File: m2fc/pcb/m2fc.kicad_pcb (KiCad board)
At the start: 4 copper layers, 100 x 70 mm, 342 parts, among them IC101 ADP3335, IC102 STM32F405VGT, IC201 AD8226, IC202 AD8656, IC203 AD8541, IC204 AD8226, IC205 AD8656, IC206 AD8541, IC207 AD8226, IC208 AD8656, IC209 AD8541, IC301 ADXL375, IC302 ADXL345, IC303 MS5611-01BA03, IC304 HMC5883L, IC305 L3G4200D, IC401 ADuM5201, IC402 ADuM1201, IC601 AD8495, IC602 AD8656, IC603 AD8495, IC604 AD8656, IC605 AD8495, IC606 AD8656, P101 CONN_2, P102 CONN_2, P103 CONN_2, P104 SWD, P201 CONN_4, P202 CONN_4, P203 CONN_4, P401 CONN_4, P402 CONN_2, P403 CONN_4, P501 CONN_2, P502 CONN_2, P503 CONN_2, P601 CONN_2, P602 CONN_2, P603 CONN_2, Q501 MOSFET_P, Q502 MOSFET_N, Q503 MOSFET_P, Q504 MOSFET_N, Q505 MOSFET_P, Q506 MOSFET_N, U106 MICROSD, X101 8M

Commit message: layout going ok so far...
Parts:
- added M3_MOUNT: VAL**, m2fc:M3_MOUNT, F.Cu at (57.8, 42.8)
- added M3_MOUNT: VAL**, m2fc:M3_MOUNT, F.Cu at (76.6, 34.4)
- added M3_MOUNT: VAL**, m2fc:M3_MOUNT, F.Cu at (126.2, 34.2)
- added M3_MOUNT: VAL**, m2fc:M3_MOUNT, F.Cu at (144.4, 45.2)
- added M3_MOUNT: VAL**, m2fc:M3_MOUNT, F.Cu at (145.4, 95.4)
- added M3_MOUNT: VAL**, m2fc:M3_MOUNT, F.Cu at (45.6, 79.2)
- moved C630 220.9 mm to (64.8, 65.4), turned to 270 degrees
- moved R607 211.6 mm to (66.2, 45.2), turned to 90 degrees
- moved C619 210.3 mm to (64.8, 54.6), turned to 270 degrees
- moved C620 206.0 mm to (74.0, 53.0), turned to 90 degrees
- moved R613 205.7 mm to (64.2, 57.2), turned to 180 degrees
- moved R618 201.6 mm to (75.6, 65.2), turned to 180 degrees
- moved C616 198.9 mm to (76.8, 53.0), turned to 90 degrees
- moved C623 197.7 mm to (68.4, 61.0), turned to 90 degrees
- moved R612 197.6 mm to (74.0, 55.8)
- moved R601 196.1 mm to (64.2, 42.6), turned to 180 degrees
- moved R603 195.4 mm to (72.6, 40.4), turned to 180 degrees
- moved C615 195.2 mm to (75.4, 53.0), turned to 90 degrees
- moved R614 194.9 mm to (66.2, 56.2), turned to 90 degrees
- moved C611 193.2 mm to (62.6, 48.0)
- moved C626 193.1 mm to (75.4, 63.8), turned to 90 degrees
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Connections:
- C611 pad 1: Net-(C608-Pad2) -> GND
- C611 pad 2: GND -> Net-(C608-Pad2)
- C622 pad 1: Net-(C619-Pad2) -> GND
- C622 pad 2: GND -> Net-(C619-Pad2)
- C633 pad 1: Net-(C630-Pad2) -> GND
- C633 pad 2: GND -> Net-(C630-Pad2)
- D407 pad 1: /IO/LED_C -> GND
- D407 pad 2: GND -> /IO/LED_C
- IC102 pad 45: Net-(IC102-Pad45) -> /IMU/GYRO_DRDY
- IC102 pad 46: /IMU/MAGNO_DRDY -> /IMU/GYRO_INT1
- IC102 pad 47: /IMU/MAGNO_SCL -> /IMU/GYRO_SCL
- IC102 pad 48: /IMU/MAGNO_SDA -> /IMU/GYRO_SDA
- IC102 pad 95: /IMU/GYRO_SCL -> /IMU/MAGNO_SCL
- IC102 pad 96: /IMU/GYRO_SDA -> /IMU/MAGNO_SDA
- IC102 pad 97: /IMU/GYRO_DRDY -> /IMU/MAGNO_DRDY
- IC102 pad 98: /IMU/GYRO_INT1 -> Net-(IC102-Pad98)
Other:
- board size 100 x 70 mm -> 108.8 x 70 mm

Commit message: about to do something dangerous to pcb
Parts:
- removed M3_MOUNT (x6): VAL**, m2fc:M3_MOUNT
- added U107: MOUNT, m2fc:M3_MOUNT, F.Cu at (45.6, 79.2)
- added U108: MOUNT, m2fc:M3_MOUNT, F.Cu at (76.6, 34.4)
- added U109: MOUNT, m2fc:M3_MOUNT, F.Cu at (126.2, 34.2)
- added U110: MOUNT, m2fc:M3_MOUNT, F.Cu at (145.4, 95.4)
- added U111: MOUNT, m2fc:M3_MOUNT, F.Cu at (144.4, 45.2)
- added U112: MOUNT, m2fc:M3_MOUNT, F.Cu at (57.8, 42.8)
- Q501, Q502, Q503, Q504, Q505, Q506: footprint m2fc:SOT-23 -> m2fc:SOT-23-MOSFET
- R505, R512, R519: moved to F.Cu
- moved R511 81.7 mm to (124.2, 70.4), turned to 270 degrees
- moved R516 81.2 mm to (131.0, 70.4), turned to 270 degrees
- moved R509 76.5 mm to (122.8, 70.4), turned to 270 degrees
- moved TP501 76.1 mm to (120.8, 81.0)
- moved TP508 73.1 mm to (132.4, 69.6)
- moved R518 71.2 mm to (132.4, 70.4), turned to 270 degrees
- moved R501 66.3 mm to (118.6, 81.0), turned to 90 degrees
- moved R510 63.9 mm to (127.4, 75.4), turned to 90 degrees
- moved R517 63.9 mm to (135.6, 75.4), turned to 90 degrees
- moved R515 63.6 mm to (134.2, 75.4), turned to 90 degrees
- moved TP505 62.5 mm to (124.2, 69.6)
- moved TP509 62.4 mm to (148.0, 102.0)
- moved TP504 61.4 mm to (128.2, 75.4)
- moved R508 60.3 mm to (126.0, 75.4), turned to 90 degrees
- moved R502 59.4 mm to (115.2, 76.0), turned to 270 degrees
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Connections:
- P102 pad 1: GND -> Net-(P102-Pad1)
- P102 pad 2: Net-(P102-Pad2) -> GND
- P103 pad 1: Net-(P102-Pad2) -> +BATT
- P103 pad 2: +BATT -> Net-(P102-Pad1)

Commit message: paid off woo
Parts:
- added C124: 2µ2, m2fc:C0603, F.Cu at (93.6, 76.8)
- added C125: 1n, m2fc:C0603, F.Cu at (88.8, 79.2)
- added C126: 2µ2, m2fc:C0603, F.Cu at (85.6, 76.8)
- added IC103: ADP3335, m2fc:MSOP8, F.Cu at (87.4, 75.8)
- added TP111: TESTPAD, m2fc:TESTPAD, F.Cu at (87.4, 75.0)
- moved R102 141.8 mm to (96.4, 75.6), turned to 270 degrees
- moved R108 137.5 mm to (90.6, 67.4), turned to 90 degrees
- moved R101 135.4 mm to (95.0, 77.2), turned to 90 degrees
- moved C116 134.8 mm to (98.4, 57.2), turned to 90 degrees
- moved C117 133.7 mm to (93.8, 70.6), turned to 180 degrees
- moved C101 130.2 mm to (93.4, 74.2)
- moved C118 126.1 mm to (93.8, 72.0), turned to 180 degrees
- moved C121 124.2 mm to (89.2, 62.8), turned to 270 degrees
- moved C115 124.0 mm to (99.0, 76.4)
- moved C110 123.0 mm to (113.2, 60.4)
- moved C123 121.8 mm to (89.2, 67.4), turned to 90 degrees
- moved C114 121.1 mm to (111.0, 77.0)
- moved C113 116.0 mm to (93.8, 69.2), turned to 180 degrees
- moved GS102 113.5 mm to (118.0, 59.0), turned to 90 degrees
- moved C122 112.4 mm to (92.2, 67.8)
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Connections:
- C117 pad 1: +3.3V -> VAA
- C118 pad 1: +3.3V -> VAA
- C204 pad 1: +3.3V -> VAA
- C205 pad 1: +3.3V -> VAA
- C206 pad 1: +3.3V -> VAA
- C209 pad 2: +3.3V -> VAA
- C210 pad 2: +3.3V -> VAA
- C211 pad 2: +3.3V -> VAA
- C212 pad 1: +3.3V -> VAA
- C213 pad 1: +3.3V -> VAA
- C217 pad 1: +3.3V -> VAA
- C218 pad 1: +3.3V -> VAA
- C219 pad 1: +3.3V -> VAA
- C222 pad 2: +3.3V -> VAA
- C223 pad 2: +3.3V -> VAA
- C224 pad 2: +3.3V -> VAA
- C225 pad 1: +3.3V -> VAA
- C226 pad 1: +3.3V -> VAA
- C230 pad 1: +3.3V -> VAA
- C231 pad 1: +3.3V -> VAA
- C232 pad 1: +3.3V -> VAA
- C235 pad 2: +3.3V -> VAA
- C236 pad 2: +3.3V -> VAA
- C237 pad 2: +3.3V -> VAA
- C238 pad 1: +3.3V -> VAA
- C239 pad 1: +3.3V -> VAA
- C601 pad 1: +3.3V -> VAA
- C602 pad 1: +3.3V -> VAA
- C604 pad 1: +3.3V -> VAA
- C605 pad 1: +3.3V -> VAA
- C612 pad 1: +3.3V -> VAA
- C613 pad 1: +3.3V -> VAA
- C615 pad 1: +3.3V -> VAA
- C616 pad 1: +3.3V -> VAA
- C623 pad 1: +3.3V -> VAA
- C624 pad 1: +3.3V -> VAA
- C626 pad 1: +3.3V -> VAA
- C627 pad 1: +3.3V -> VAA
- D201 pad 2: +3.3V -> VAA
- D203 pad 2: +3.3V -> VAA
- D205 pad 2: +3.3V -> VAA
- IC102 pad 21: +3.3V -> VAA
- IC102 pad 22: +3.3V -> VAA
- IC102 pad 69: Net-(IC102-Pad69) -> /SJ1
- IC102 pad 7: /SJ1 -> Net-(IC102-Pad7)
- IC102 pad 70: Net-(IC102-Pad70) -> /SJ2
- IC102 pad 71: Net-(IC102-Pad71) -> /SJ3
- IC102 pad 8: /SJ2 -> Net-(IC102-Pad8)
- IC102 pad 9: /SJ3 -> Net-(IC102-Pad9)
- IC201 pad 8: +3.3V -> VAA
- IC202 pad 4: +3.3V -> VAA
- IC203 pad 5: +3.3V -> VAA
- IC204 pad 8: +3.3V -> VAA
- IC205 pad 4: +3.3V -> VAA
- IC206 pad 5: +3.3V -> VAA
- IC207 pad 8: +3.3V -> VAA
- IC208 pad 4: +3.3V -> VAA
- IC209 pad 5: +3.3V -> VAA
- IC601 pad 7: +3.3V -> VAA
- IC602 pad 4: +3.3V -> VAA
- IC603 pad 7: +3.3V -> VAA
- IC604 pad 4: +3.3V -> VAA
- IC605 pad 7: +3.3V -> VAA
- IC606 pad 4: +3.3V -> VAA
- P201 pad 4: +3.3V -> VAA
- P202 pad 4: +3.3V -> VAA
- P203 pad 4: +3.3V -> VAA
- R202 pad 1: +3.3V -> VAA
- R210 pad 1: +3.3V -> VAA
- R218 pad 1: +3.3V -> VAA

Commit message: omg layout done
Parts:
- moved C301 131.3 mm to (95.6, 83.2)
- moved R304 129.4 mm to (93.4, 59.8), turned to 90 degrees
- moved R301 129.1 mm to (102.2, 83.2), turned to 90 degrees
- moved C310 126.0 mm to (105.2, 80.2), turned to 180 degrees
- moved C314 122.6 mm to (89.2, 55.8), turned to 90 degrees
- moved C302 121.6 mm to (100.2, 83.2), turned to 180 degrees
- moved R306 119.3 mm to (94.8, 59.8), turned to 90 degrees
- moved C307 119.1 mm to (101.4, 55.8), turned to 90 degrees
- moved R307 117.1 mm to (108.0, 56.0), turned to 90 degrees
- moved R305 115.7 mm to (103.6, 81.6)
- moved C312 114.6 mm to (90.6, 54.2), turned to 270 degrees
- moved TP303 113.5 mm to (99.0, 77.6)
- moved C313 109.3 mm to (108.0, 76.8), turned to 270 degrees
- moved C311 108.8 mm to (109.4, 76.8), turned to 270 degrees
- moved TP307 108.7 mm to (103.0, 76.8)
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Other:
- board size 108.8 x 70 mm -> 100 x 70 mm

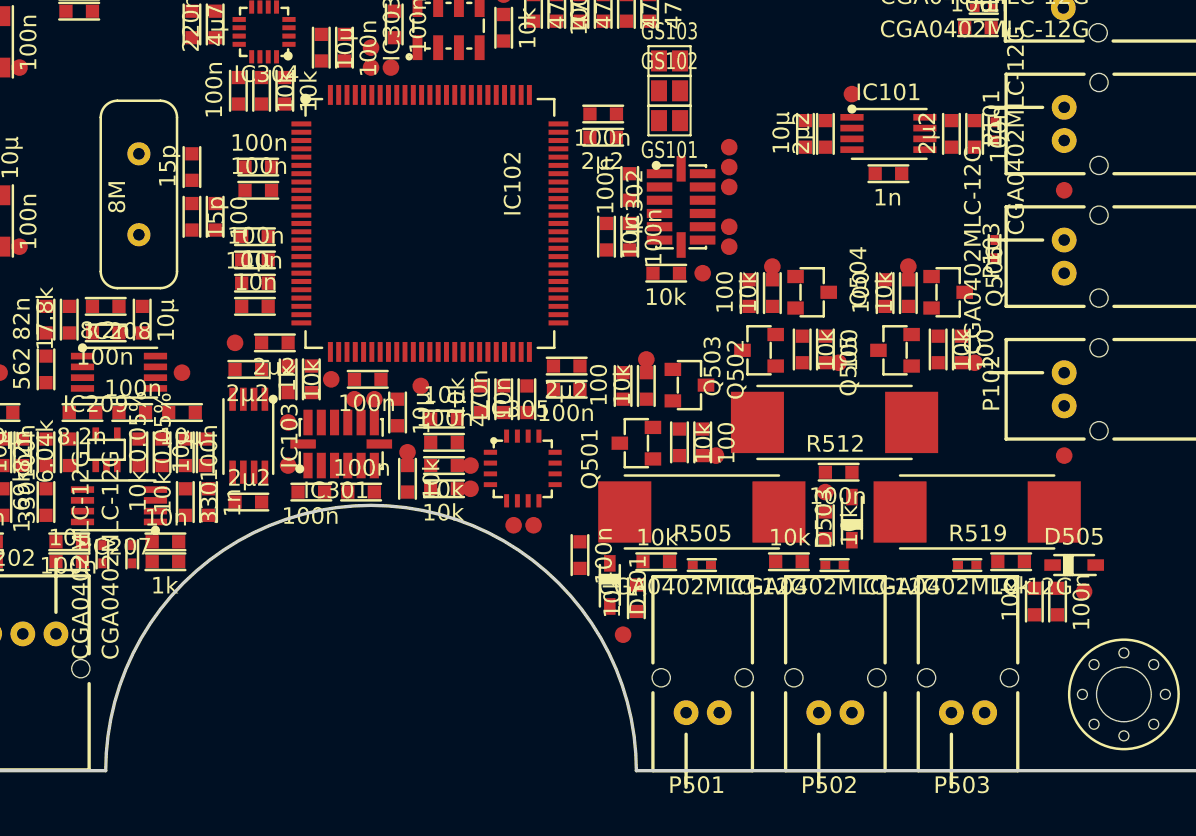
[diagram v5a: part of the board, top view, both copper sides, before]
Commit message: swap crystal to smt. ready 2 route!!
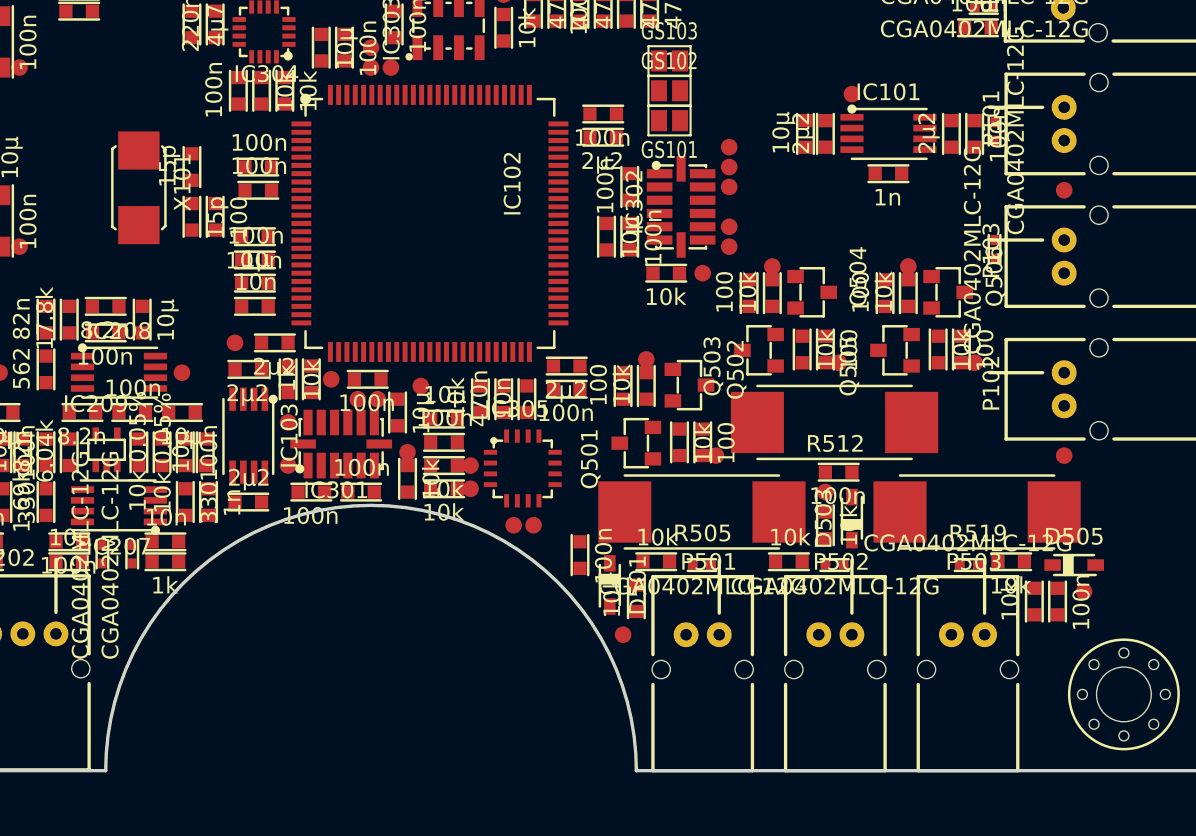
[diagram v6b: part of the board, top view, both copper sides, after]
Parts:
- X101: footprint m2fc:HC49S -> m2fc:XTAL50x32
- moved P501 5.11 mm to (121.0, 91.8), turned to 180 degrees
- moved P502 5.11 mm to (129.0, 91.8), turned to 180 degrees
- moved P503 5.11 mm to (137.0, 91.8), turned to 180 degrees
- moved D506 1.20 mm to (136.6, 87.6), turned to 180 degrees
- moved TP301 0.20 mm to (100.4, 77.6)
- moved TP303 0.20 mm to (99.2, 77.6)
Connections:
- IC102 pad 4: /IO/LED_A -> Net-(IC102-Pad4)
- IC102 pad 5: /IO/LED_C -> Net-(IC102-Pad5)
- IC102 pad 59: /IO/LED_1 -> Net-(IC102-Pad59)
- IC102 pad 60: /IO/LED_2 -> /SJ1
- IC102 pad 61: /IO/LED_3 -> /SJ2
- IC102 pad 62: /IO/LED_4 -> /SJ3
- IC102 pad 63: Net-(IC102-Pad63) -> /IO/LED_C
- IC102 pad 64: Net-(IC102-Pad64) -> /IO/LED_A
- IC102 pad 68: Net-(IC102-Pad68) -> /IO/LED_1
- IC102 pad 69: /SJ1 -> /IO/LED_2
- IC102 pad 70: /SJ2 -> /IO/LED_3
- IC102 pad 71: /SJ3 -> /IO/LED_4

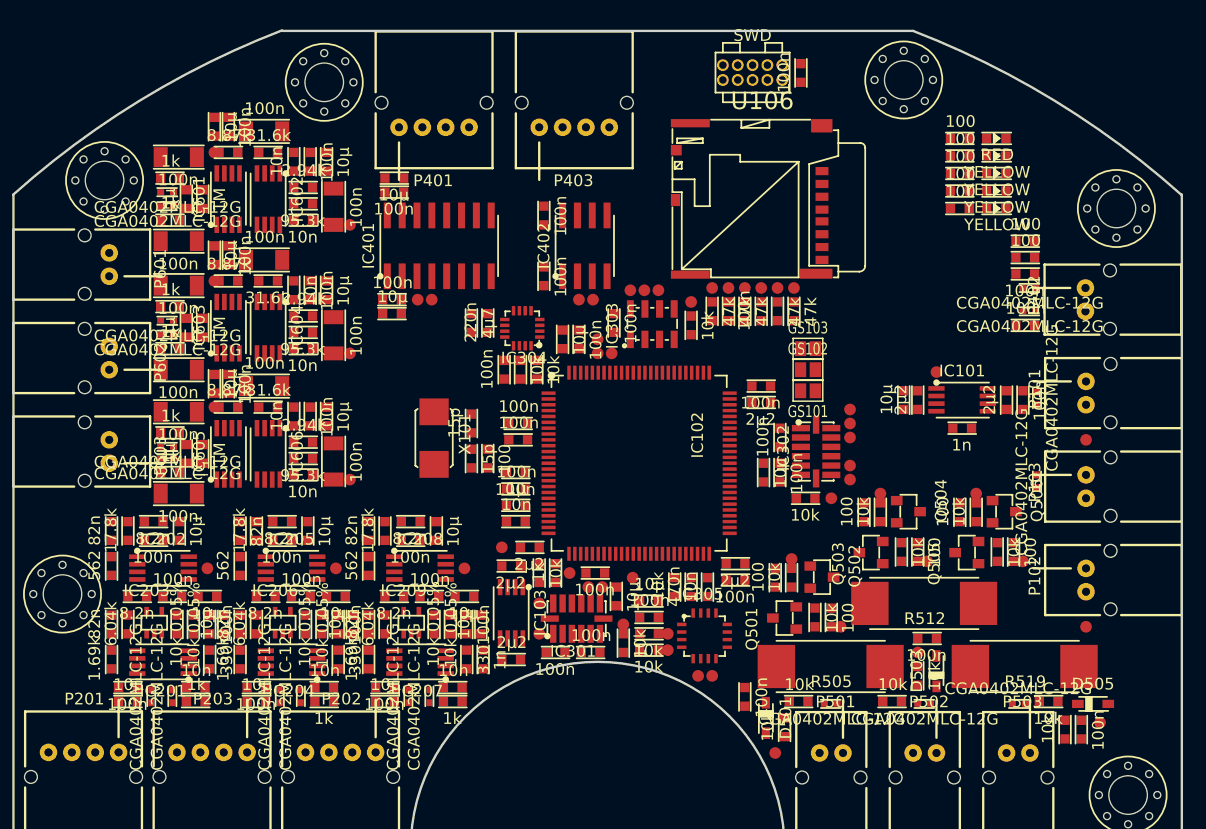
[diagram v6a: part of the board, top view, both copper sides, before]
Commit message: analogue section routed woop woop
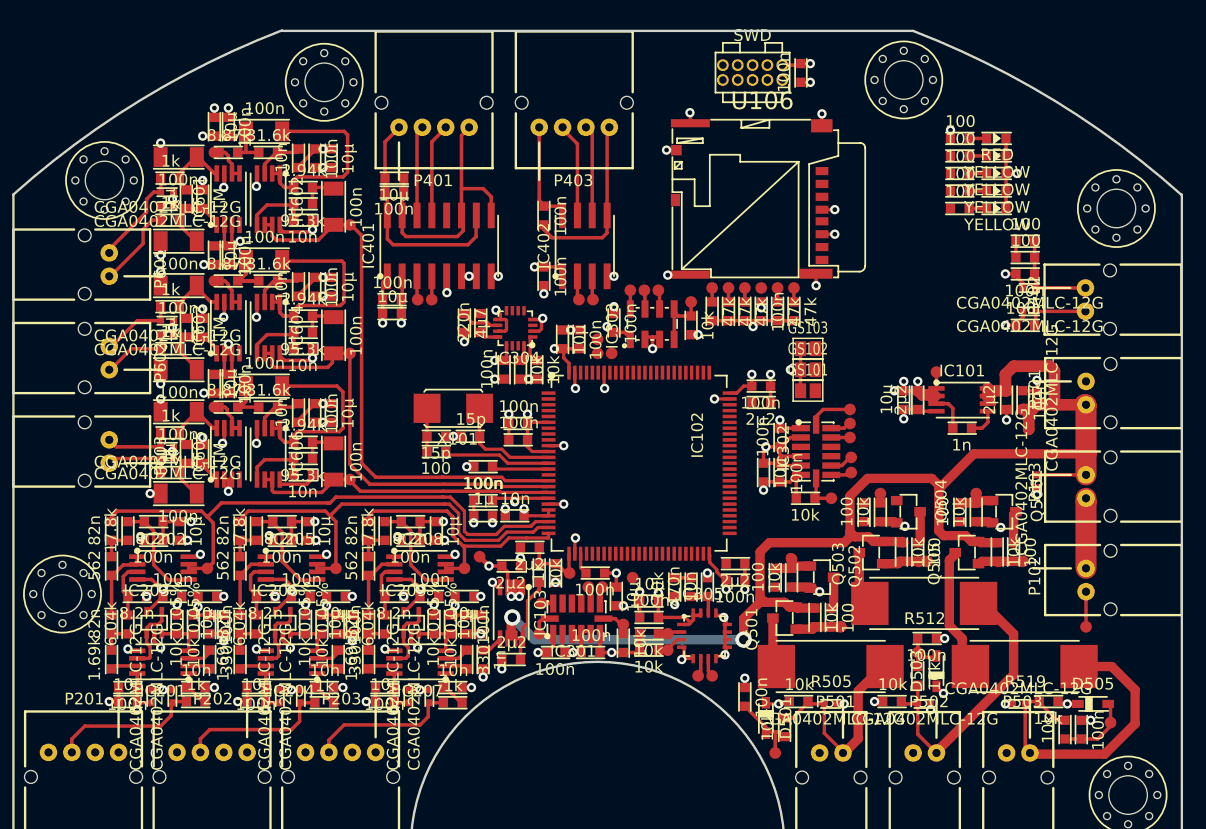
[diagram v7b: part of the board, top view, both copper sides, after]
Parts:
- moved P202 11.0 mm to (70.0, 91.8)
- moved P203 11.0 mm to (81.0, 91.8)
- moved R108 5.39 mm to (85.4, 66.0), turned to 0 degrees
- moved TP104 4.98 mm to (136.9, 64.1)
- moved C123 4.66 mm to (85.4, 64.7), turned to 0 degrees
- moved X101 3.73 mm to (89.7, 62.3), turned to 180 degrees
- moved C113 2.97 mm to (91.0, 70.2)
- moved C117 2.94 mm to (91.0, 71.5)
- moved C122 2.84 mm to (89.4, 67.3)
- moved TP111 2.06 mm to (89.9, 75.0)
- moved C121 2.02 mm to (89.9, 64.7), turned to 180 degrees
- moved C620 1.94 mm to (74.4, 51.1), turned to 270 degrees
- moved R209 1.60 mm to (77.4, 87.5), turned to 180 degrees
- moved R217 1.60 mm to (88.4, 87.5), turned to 180 degrees
- moved C108 1.60 mm to (114.0, 54.8), turned to 90 degrees
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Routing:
- net GND: track 0.00 -> 217.6 mm, vias 0 -> 116
- net +BATT: track 0.00 -> 124.6 mm, vias 0 -> 2
- net +3.3V: track 0.00 -> 106.8 mm, vias 0 -> 31
- net VAA: track 0.00 -> 83.5 mm, vias 0 -> 33
- net /StrainGauges/STRAIN_1: track 0.00 -> 48.9 mm
- net /Thermocouples/THERMO_1: track 0.00 -> 46.5 mm
- net /StrainGauges/STRAIN_2: track 0.00 -> 37.2 mm
- net /Thermocouples/THERMO_2: track 0.00 -> 36.6 mm
- net Net-(D506-Pad1): track 0.00 -> 27.6 mm
- net /Thermocouples/THERMO_3: track 0.00 -> 26.6 mm
- net Net-(D504-Pad1): track 0.00 -> 25.7 mm
- net Net-(C402-Pad2): track 0.00 -> 24.1 mm
- net /StrainGauges/STRAIN_3: track 0.00 -> 24.0 mm
- net Net-(C402-Pad1): track 0.00 -> 20.8 mm
- net Net-(D502-Pad1): track 0.00 -> 18.2 mm
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- added copper zone on In2.Cu, net +3.3V
- added copper zone on In1.Cu, net GND
- added copper zone on In2.Cu, net VAA

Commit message: routing continues
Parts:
- removed GS103: GS2, Connect:GS2
- removed TP322, TP323: TESTPAD, m2fc:TESTPAD
- moved TP109 38.1 mm to (144.8, 31.6)
- moved TP106 38.1 mm to (149.0, 31.6)
- moved TP107 38.1 mm to (142.0, 31.6)
- moved TP108 38.1 mm to (143.4, 31.6)
- moved TP105 38.1 mm to (147.6, 31.6)
- moved TP110 38.1 mm to (146.2, 31.6)
- moved D401 20.7 mm to (125.8, 58.5)
- moved R401 20.7 mm to (124.2, 58.5)
- moved C109 18.1 mm to (115.0, 59.4)
- moved TP321 17.8 mm to (93.0, 43.6)
- moved R307 17.2 mm to (96.2, 43.5), turned to 180 degrees
- moved D402 14.0 mm to (125.8, 57.0)
- moved D403 14.0 mm to (125.8, 55.5)
- moved D404 14.0 mm to (125.8, 54.0)
- moved D405 14.0 mm to (125.8, 52.5)
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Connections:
- IC102 pad 33: /IMU/HG_ACCEL_INT1 -> /IMU/HG_ACCEL_INT2
- IC102 pad 34: /IMU/HG_ACCEL_INT2 -> /IMU/HG_ACCEL_INT1
- IC102 pad 44: Net-(IC102-Pad44) -> /IMU/GYRO_INT1
- IC102 pad 46: /IMU/GYRO_INT1 -> Net-(IC102-Pad46)
- IC102 pad 62: /SJ3 -> Net-(IC102-Pad62)
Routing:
- net /IO/SER_OUT_1: track 2.06 -> 27.5 mm
- net GND: track 217.6 -> 194.9 mm, vias 116 -> 96
- net /IO/SER_IN_2: track 2.22 -> 24.5 mm
- net /IO/SER_IN_1: track 2.15 -> 22.2 mm
- net /IMU/BARO_MOSI: track 2.02 -> 21.5 mm
- net /IMU/BARO_CS: track 5.47 -> 24.0 mm
- net /IMU/BARO_MISO: track 1.84 -> 20.0 mm
- net +3.3V: track 106.8 -> 90.4 mm, vias 31 -> 22
- net /IMU/BARO_SCK: track 2.01 -> 18.2 mm, vias 0 -> 2
- net /IMU/MAGNO_SCL: track 2.30 -> 13.5 mm
- net /IMU/MAGNO_DRDY: track 0.00 -> 9.33 mm
- net /IMU/HG_ACCEL_INT1: track 1.69 -> 10.9 mm
- net /IO/SER_OUT_2: track 2.20 -> 10.7 mm
- net /IMU/MAGNO_SDA: track 1.64 -> 10.1 mm
- net /IMU/HG_ACCEL_INT2: track 1.89 -> 9.96 mm
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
